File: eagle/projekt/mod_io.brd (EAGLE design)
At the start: 102.5 x 80 mm, 47 parts, among them IC1 PCF8574P

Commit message: Deska mod IO
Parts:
- moved R17 32.9 mm to (83.8, 68.6), turned to 270 degrees
- moved R18 21.6 mm to (71.1, 44.5)
- moved R14 6.35 mm to (44.5, 31.8), turned to 270 degrees
- moved C1 2.54 mm to (59.7, 67.3)
- moved R16 2.54 mm to (77.5, 39.4)
- moved R1 1.27 mm to (14.0, 26.7)
- moved IO1 1.27 mm to (7.62, 49.5)
- moved CNF 1.27 mm to (21.6, 61.0)
- moved IO2 1.27 mm to (31.8, 72.4)
- moved INT 0.63 mm to (31.8, 61.6)
- moved SCL 0.63 mm to (41.9, 61.6)
- moved SDA 0.63 mm to (36.8, 61.6)
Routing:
- net GND: track 0.00 -> 321.9 mm
- net VCC: track 0.00 -> 312.8 mm
- net N$4: track 0.00 -> 286.2 mm
- net N$3: track 0.00 -> 245.1 mm
- net N$5: track 0.00 -> 243.5 mm
- net GPIO5: track 0.00 -> 154.1 mm
- net GPIO3: track 0.00 -> 150.3 mm
- net N$6: track 0.00 -> 145.4 mm
- net N$2: track 0.00 -> 128.0 mm
- net N$7: track 0.00 -> 122.6 mm
- net N$17: track 0.00 -> 116.9 mm
- net N$8: track 0.00 -> 110.6 mm
- net GPIO14: track 0.00 -> 107.1 mm, vias 0 -> 3
- net GPIO13: track 0.00 -> 100.7 mm
- net N$23: track 0.00 -> 88.9 mm
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
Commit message: Deska, modul IO
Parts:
- moved D6 0.32 mm to (70.2, 21.6)
- moved D7 0.32 mm to (82.9, 21.6)
- moved R17 0.32 mm to (84.1, 68.6)
- moved R7 0.32 mm to (87.9, 26.7)
- moved S6 0.32 mm to (70.2, 10.2)
- moved S7 0.32 mm to (82.9, 10.2)
- moved A1 0.32 mm to (57.5, 71.1)
- moved A2 0.32 mm to (62.5, 71.1)
- moved C1 0.32 mm to (60.0, 67.3)
- moved D3 0.32 mm to (32.1, 21.6)
- moved D5 0.32 mm to (57.5, 21.6)
- moved INT 0.32 mm to (32.1, 61.6)
- moved IO2 0.32 mm to (32.1, 72.4)
- moved R10 0.32 mm to (32.1, 31.8)
- moved R13 0.32 mm to (63.8, 35.6)
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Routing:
- net GPIO5: track 154.1 -> 157.2 mm
- net GPIO3: track 150.3 -> 152.5 mm
- net N$2: track 128.0 -> 129.9 mm
- net N$5: track 243.5 -> 245.3 mm
- net N$1: track 85.0 -> 86.5 mm
- net GPIO1: track 86.1 -> 87.5 mm
- net GPIO13: track 100.7 -> 101.8 mm
- net VCC: track 312.8 -> 313.9 mm
- net N$6: track 145.4 -> 146.5 mm
- net N$17: track 116.9 -> 116.0 mm
- net N$7: track 122.6 -> 122.0 mm
- net VIN: track 71.4 -> 72.0 mm
- net ADC: track 75.8 -> 75.2 mm
- added copper zone on layer 1, net N$24
- added copper zone on layer 16, net N$26
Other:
- board size 102.5 x 80 mm -> 103.2 x 80 mm
- board text added: "IO 6/17"
- board text added: "by MVa"

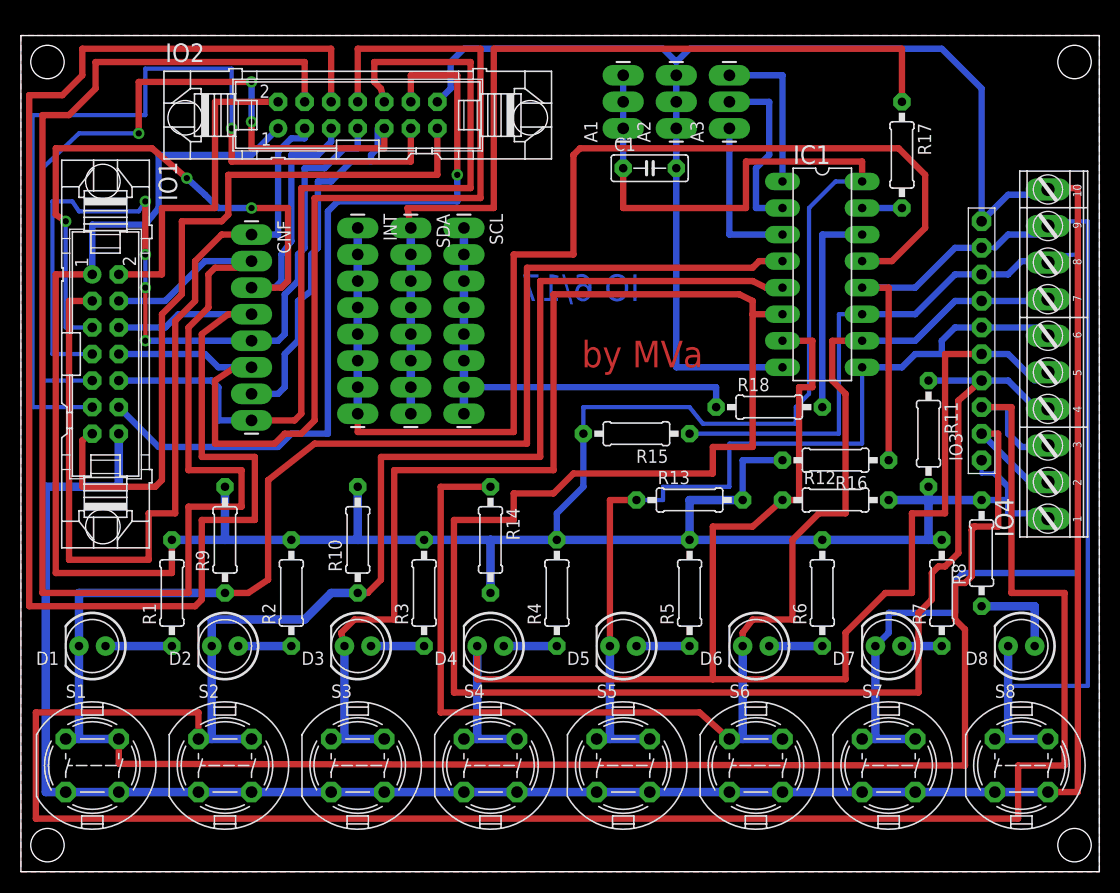
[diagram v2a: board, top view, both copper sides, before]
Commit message: Modul IO deska podklady
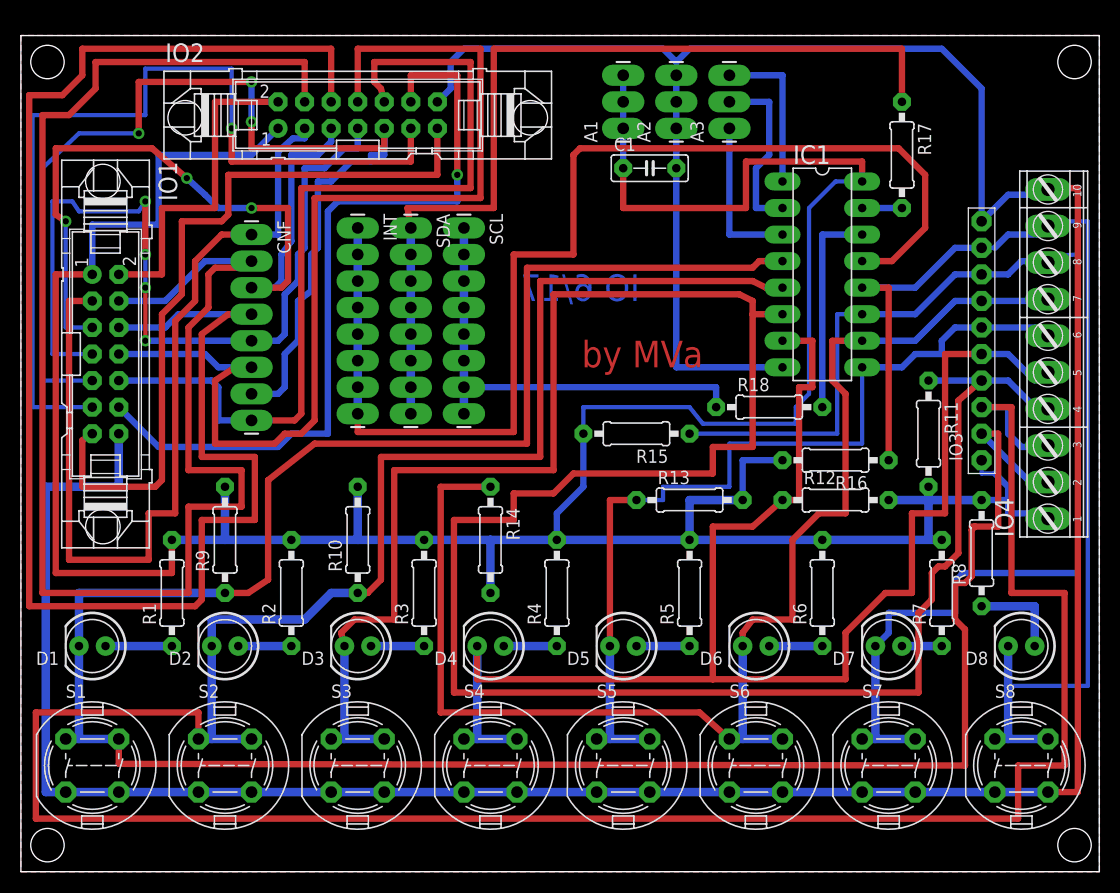
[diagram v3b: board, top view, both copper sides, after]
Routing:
- net VCC: track 313.9 -> 314.7 mm
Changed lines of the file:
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@@
 <?xml version="1.0" encoding="utf-8"?>
 <!DOCTYPE eagle SYSTEM "eagle.dtd">
-<eagle version="7.3.0">
+<eagle version="7.5.0">
 <drawing>
 <settings>
@@
 <param name="mdSmdStop" value="0mil"/>
 <param name="msWidth" value="10mil"/>
-<param name="msDrill" value="24mil"/>
+<param name="msDrill" value="20mil"/>
 <param name="msMicroVia" value="9.99mm"/>
 <param name="msBlindViaRatio" value="0.5"/>
@@
 <param name="rvMicroViaOuter" value="0.25"/>
 <param name="rvMicroViaInner" value="0.25"/>
-<param name="rlMinPadTop" value="17mil"/>
+<param name="rlMinPadTop" value="18mil"/>
 <param name="rlMaxPadTop" value="20mil"/>
 <param name="rlMinPadInner" value="10mil"/>
 <param name="rlMaxPadInner" value="20mil"/>
-<param name="rlMinPadBottom" value="17mil"/>
+<param name="rlMinPadBottom" value="18mil"/>
 <param name="rlMaxPadBottom" value="20mil"/>
 <param name="rlMinViaOuter" value="10mil"/>
@@
 <wire x1="89.2175" y1="57.15" x2="85.4075" y2="53.34" width="0.6096" layer="16"/>
 <wire x1="85.4075" y1="53.34" x2="80.3275" y2="53.34" width="0.6096" layer="16"/>
-<wire x1="63.8175" y1="41.91" x2="78.105" y2="41.91" width="0.4064" layer="16"/>
-<wire x1="78.105" y1="41.91" x2="78.105" y2="53.34" width="0.4064" layer="16"/>
-<wire x1="78.105" y1="53.34" x2="80.3275" y2="53.34" width="0.4064" layer="16"/>
+<wire x1="63.8175" y1="41.91" x2="77.94625" y2="41.91" width="0.4064" layer="16"/>
+<wire x1="77.94625" y1="41.91" x2="77.94625" y2="53.34" width="0.4064" layer="16"/>
+<wire x1="77.94625" y1="53.34" x2="80.3275" y2="53.34" width="0.4064" layer="16"/>
 <wire x1="81.5975" y1="21.59" x2="82.8675" y2="22.86" width="0.6096" layer="16"/>
 <wire x1="82.8675" y1="22.86" x2="82.8675" y2="24.765" width="0.6096" layer="16"/>
@@
 <wire x1="91.7575" y1="35.56" x2="86.6775" y2="35.56" width="0.8128" layer="16"/>
 <wire x1="6.6675" y1="57.15" x2="6.6675" y2="61.9125" width="0.6096" layer="16"/>
-<wire x1="6.6675" y1="61.9125" x2="11.7475" y2="61.9125" width="0.6096" layer="16"/>
-<wire x1="11.7475" y1="61.9125" x2="13.0175" y2="63.5" width="0.6096" layer="16"/>
-<wire x1="13.0175" y1="63.5" x2="13.0175" y2="68.58" width="0.6096" layer="16"/>
+<wire x1="6.6675" y1="61.9125" x2="13.0175" y2="61.9125" width="0.6096" layer="16"/>
+<wire x1="13.0175" y1="61.9125" x2="13.0175" y2="68.58" width="0.6096" layer="16"/>
 <wire x1="13.0175" y1="68.58" x2="21.9075" y2="68.58" width="0.6096" layer="16"/>
 <wire x1="21.9075" y1="68.58" x2="24.4475" y2="71.12" width="0.6096" layer="16"/>
@@
 <wire x1="4.445" y1="54.61" x2="6.6675" y2="54.61" width="0.6096" layer="1"/>
 <wire x1="26.9875" y1="71.12" x2="26.9875" y2="70.1675" width="0.6096" layer="16"/>
-<wire x1="26.9875" y1="70.1675" x2="25.7175" y2="70.1675" width="0.6096" layer="16"/>
-<wire x1="25.7175" y1="70.1675" x2="24.4475" y2="68.8975" width="0.6096" layer="16"/>
+<wire x1="26.9875" y1="70.1675" x2="25.87625" y2="70.1675" width="0.6096" layer="16"/>
+<wire x1="25.87625" y1="70.1675" x2="24.4475" y2="68.8975" width="0.6096" layer="16"/>
 </signal>
 <signal name="GPIO4">
@@
 <wire x1="31.4325" y1="67.945" x2="33.3375" y2="67.945" width="0.6096" layer="16"/>
 <wire x1="33.3375" y1="67.945" x2="33.3375" y2="68.58" width="0.6096" layer="16"/>
-<wire x1="33.3375" y1="68.58" x2="33.9725" y2="69.215" width="0.6096" layer="16"/>
-<wire x1="33.9725" y1="69.215" x2="33.9725" y2="71.12" width="0.6096" layer="16"/>
-<wire x1="33.9725" y1="71.12" x2="34.6075" y2="71.12" width="0.4064" layer="16"/>
+<wire x1="33.3375" y1="68.58" x2="34.6075" y2="68.58" width="0.6096" layer="16"/>
+<wire x1="34.6075" y1="68.58" x2="34.6075" y2="70.485" width="0.6096" layer="16"/>
+<wire x1="34.6075" y1="70.485" x2="34.6075" y2="71.12" width="0.4064" layer="16"/>
 <wire x1="6.6675" y1="46.99" x2="1.905" y2="46.99" width="0.4064" layer="16"/>
 <wire x1="1.905" y1="46.99" x2="1.905" y2="67.31" width="0.4064" layer="16"/>
